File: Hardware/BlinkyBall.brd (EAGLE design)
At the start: 4 parts, among them IC3 TINY13-20SSU

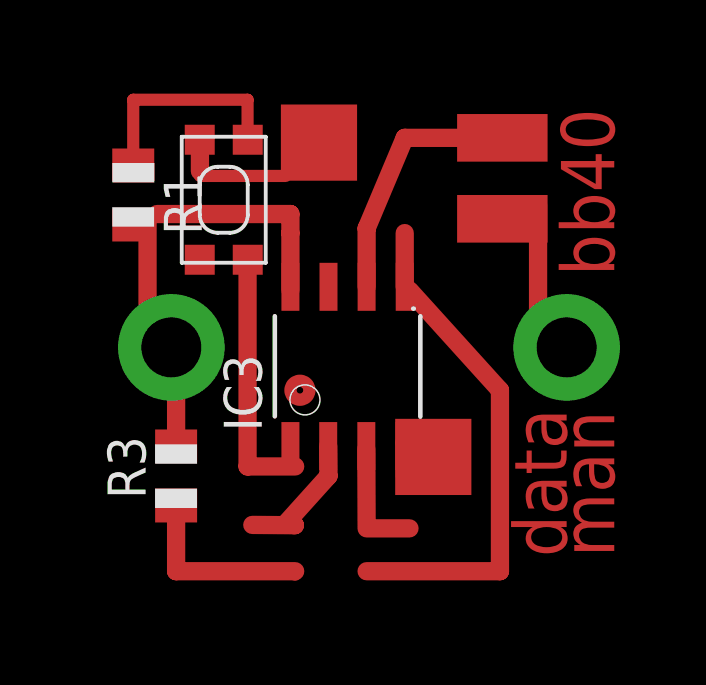
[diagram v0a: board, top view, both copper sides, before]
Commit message: Revisions to board
Duh, I had used int1 rather than int0.  No wonder tilt switch did not
work.  I guess you need to get away from a project to see it clearly
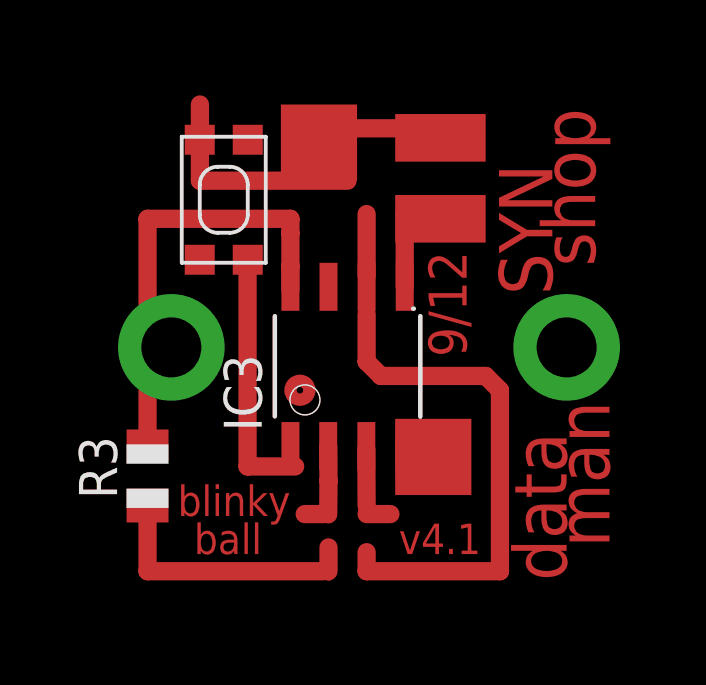
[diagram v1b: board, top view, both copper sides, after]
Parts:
- removed R1: (no value), adafruit:R0805
- moved R3 0.95 mm to (3.33, 5.71)
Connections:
- removed net N$29: IC3.6
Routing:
- net S$11: track 0.00 -> 17.5 mm
- net S$8: track 15.0 -> 0.63 mm
- net N$29: track 7.76 -> 0.00 mm
- net S$5: track 6.67 -> 0.00 mm
- net S$1: track 1.90 -> 7.46 mm
- net S$6: track 2.86 -> 0.00 mm
- net N$25: track 1.79 -> 4.65 mm
- net N$26: track 4.89 -> 2.28 mm
- net S$12: track 0.00 -> 2.06 mm
- net N$28: track 6.26 -> 8.24 mm
- net S$4: track 8.29 -> 10.0 mm
- net S$9: track 1.11 -> 0.00 mm
- net S$13: track 0.00 -> 0.79 mm
- net S$2: track 5.08 -> 5.71 mm
- net N$27: track 2.63 -> 1.99 mm
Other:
- board text added: "9/12"
- board text added: "SYN"
- board text added: "ball"
- board text added: "blinky"
- board text added: "shop"
- board text added: "v4.1"
- board text removed: "bb40"

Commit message: tinkering
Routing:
- net N$25: track 4.65 -> 0.00 mm
- net S$5: track 0.00 -> 2.54 mm
- net S$11: track 17.5 -> 19.2 mm
- net S$13: track 0.79 -> 1.59 mm
- net S$6: track 0.00 -> 0.79 mm
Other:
- board text added: "4"
- board text added: "Padi"
- board text added: "all"
- board text added: "wan"
- board text removed: "ball"
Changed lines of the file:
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@@
 <board>
 <plain>
-<circle x="8.41375" y="8.5725" radius="0.3175" width="0.4064" layer="1"/>
-<text x="13.97" y="9.68375" size="1.27" layer="1" rot="R90">9/12</text>
-<circle x="13.49375" y="14.12875" radius="0.3175" width="0.4064" layer="16"/>
+<circle x="8.09625" y="7.62" radius="0.3175" width="0.254" layer="1"/>
+<text x="14.605" y="9.2075" size="1.6764" layer="1" rot="R90">9/12</text>
+<circle x="13.17625" y="14.76375" radius="0.3175" width="0.4064" layer="16"/>
 <rectangle x1="7.77875" y1="15.5575" x2="10.31875" y2="18.0975" layer="1"/>
 <rectangle x1="11.58875" y1="5.08" x2="14.12875" y2="7.62" layer="1"/>
 <rectangle x1="11.58875" y1="16.1925" x2="14.605" y2="17.78" layer="1"/>
-<rectangle x1="11.58875" y1="13.49375" x2="14.605" y2="15.08125" layer="1"/>
+<rectangle x1="11.58875" y1="14.12875" x2="14.605" y2="15.71625" layer="1"/>
 <text x="16.8275" y="11.7475" size="1.778" layer="1" rot="R90">SYN</text>
 <text x="18.7325" y="3.33375" size="1.778" layer="1" rot="R90">man</text>
-<text x="8.09625" y="5.3975" size="1.016" layer="1" rot="R180">blinky</text>
-<text x="7.14375" y="4.1275" size="1.016" layer="1" rot="R180">ball</text>
-<text x="14.44625" y="4.1275" size="1.016" layer="1" rot="R180">v4.1</text>
+<text x="4.445" y="7.62" size="1.27" layer="1" rot="R270">blinky</text>
+<text x="7.62" y="4.445" size="1.27" layer="1" rot="R180">all</text>
+<text x="14.605" y="4.60375" size="1.016" layer="1" rot="R180">v4.1</text>
 <text x="18.25625" y="12.7" size="1.778" layer="1" rot="R90">shop</text>
 <text x="17.30375" y="2.2225" size="1.778" layer="1" rot="R90">data</text>
+<text x="11.1125" y="10.63625" size="1.27" layer="1" rot="R180">Padi</text>
+<text x="11.43" y="9.36625" size="1.27" layer="1" rot="R180">wan</text>
+<text x="9.8425" y="14.76375" size="1.27" layer="1" rot="R180">4</text>
+<rectangle x1="3.175" y1="15.39875" x2="4.1275" y2="18.25625" layer="1"/>
 </plain>
 <attributes>
@@
 <signal name="N$25">
 <contactref element="IC3" pad="5"/>
-<wire x1="11.90625" y1="12.02025" x2="11.90625" y2="14.44625" width="0.6096" layer="1"/>
-<wire x1="11.90625" y1="14.44625" x2="14.12875" y2="14.44625" width="0.6096" layer="1"/>
+<wire x1="11.90625" y1="12.02025" x2="11.90625" y2="14.2875" width="0" layer="19" extent="1-16"/>
+<wire x1="11.90625" y1="14.2875" x2="14.12875" y2="14.44625" width="0" layer="19" extent="1-16"/>
 </signal>
 <signal name="N$26">
@@
 <signal name="S$2">
 <wire x1="10.63625" y1="4.445" x2="11.43" y2="4.445" width="0.6096" layer="1"/>
-<wire x1="9.36625" y1="17.30375" x2="14.2875" y2="17.30375" width="0.6096" layer="1"/>
+<wire x1="9.36625" y1="17.78" x2="14.2875" y2="17.78" width="0.6096" layer="1"/>
 </signal>
 <signal name="S$3">
@@
 <signal name="S$7">
 <wire x1="6.6675" y1="12.85875" x2="6.6675" y2="6.0325" width="0.6096" layer="1"/>
-<wire x1="6.6675" y1="6.0325" x2="8.255" y2="6.0325" width="0.6096" layer="1"/>
+<wire x1="6.6675" y1="6.0325" x2="8.09625" y2="6.0325" width="0.6096" layer="1"/>
 </signal>
 <signal name="S$10">
@@
 </signal>
 <signal name="S$11">
-<wire x1="10.63625" y1="11.1125" x2="10.63625" y2="9.525" width="0.6096" layer="1"/>
-<wire x1="10.63625" y1="9.525" x2="11.1125" y2="9.04875" width="0.6096" layer="1"/>
+<wire x1="11.90625" y1="13.49375" x2="11.90625" y2="8.5725" width="0.6096" layer="1"/>
 <wire x1="15.08125" y1="8.5725" x2="15.08125" y2="2.54" width="0.6096" layer="1"/>
 <wire x1="15.08125" y1="2.54" x2="10.63625" y2="2.54" width="0.6096" layer="1"/>
-<wire x1="11.1125" y1="9.04875" x2="14.605" y2="9.04875" width="0.6096" layer="1"/>
-<wire x1="14.605" y1="9.04875" x2="15.08125" y2="8.5725" width="0.6096" layer="1"/>
+<wire x1="11.90625" y1="8.5725" x2="15.08125" y2="8.5725" width="0.6096" layer="1"/>
 <wire x1="10.63625" y1="2.54" x2="10.63625" y2="3.175" width="0.6096" layer="1"/>
 </signal>
 <signal name="S$12">
-<wire x1="10.63625" y1="12.3825" x2="10.63625" y2="14.44625" width="0.6096" layer="1"/>
+<wire x1="10.63625" y1="12.3825" x2="10.63625" y2="14.2875" width="0.6096" layer="1"/>
 </signal>
 <signal name="S$8">
@@
 <signal name="S$13">
 <wire x1="9.36625" y1="2.54" x2="9.36625" y2="3.33375" width="0.6096" layer="1"/>
+<wire x1="9.36625" y1="3.33375" x2="8.5725" y2="3.33375" width="0.6096" layer="1"/>
 </signal>
 <signal name="S$1">
@@
 <wire x1="5.08" y1="15.5575" x2="5.08" y2="18.0975" width="0.6096" layer="1"/>
 </signal>
+<signal name="S$5">
+<wire x1="10.63625" y1="14.44625" x2="13.17625" y2="14.44625" width="0.6096" layer="1"/>
+</signal>
+<signal name="S$6">
+<wire x1="10.63625" y1="3.33375" x2="11.43" y2="3.33375" width="0.6096" layer="1"/>
+</signal>
 </signals>
